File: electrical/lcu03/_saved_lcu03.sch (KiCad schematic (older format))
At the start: 94 parts, among them P1 screw, P10 swd, P11 stepper_conn, P12 stepper_conn, P13 stepper_conn, P16 screw, P17 screw, P2 screw, P3 screw, P4 screw, P5 ext-1, P6 ~rst~, P7 mode, P8 ext-2, P9 USB_B, Q1 bc857, Q2 bc847, Q3 bc857, Q4 ntd18n06l, U1 crystal-4pin, U2 CP2102, U3 m24c02, U4 NCP3063, U6 ts881, U7 lb1930mc

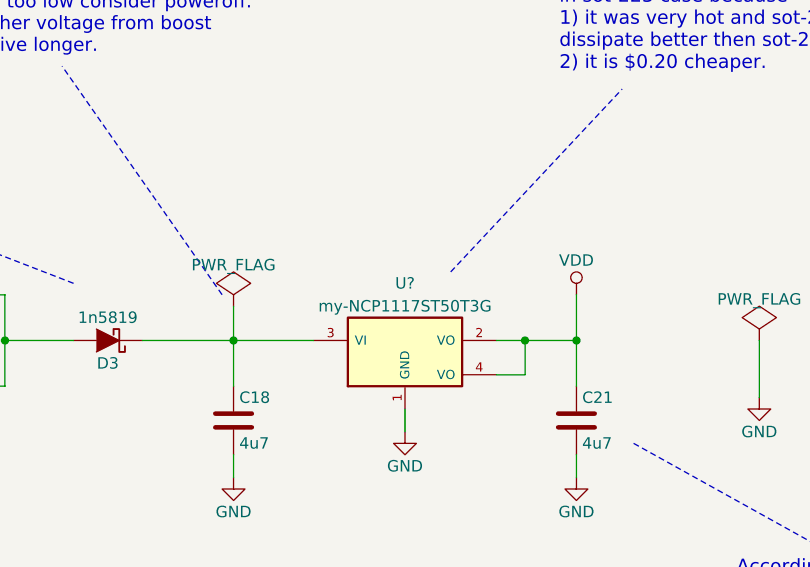
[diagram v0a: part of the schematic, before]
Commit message: Replaced linear regulator, changed socket footprints and implemented all improvements from "zzz.txt" file.
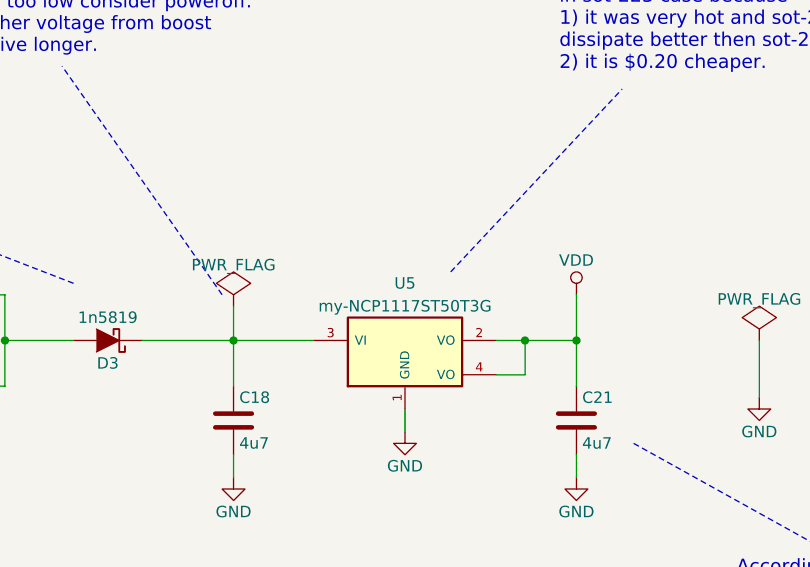
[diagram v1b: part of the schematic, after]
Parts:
- U5: renamed from U?; footprint (none) -> TO_SOT_Packages_SMD:SOT-223
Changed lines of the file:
@@
 According to datasheet \nthis one is mandatory \nfor stability.
 $Comp
-L my-NCP1117ST50T3G U?
+L my-NCP1117ST50T3G U5
 U 1 1 56BBB7F9
 P 15300 17250
-F 0 "U?" H 15300 17550 50  0000 C CNN
+F 0 "U5" H 15300 17550 50  0000 C CNN
 F 1 "my-NCP1117ST50T3G" H 15300 17450 50  0000 C CNN
-F 2 "" H 15300 17250 50  0000 C CNN
+F 2 "TO_SOT_Packages_SMD:SOT-223" H 15300 17250 50  0001 C CNN
 F 3 "" H 15300 17250 50  0000 C CNN
 	1    15300 17250

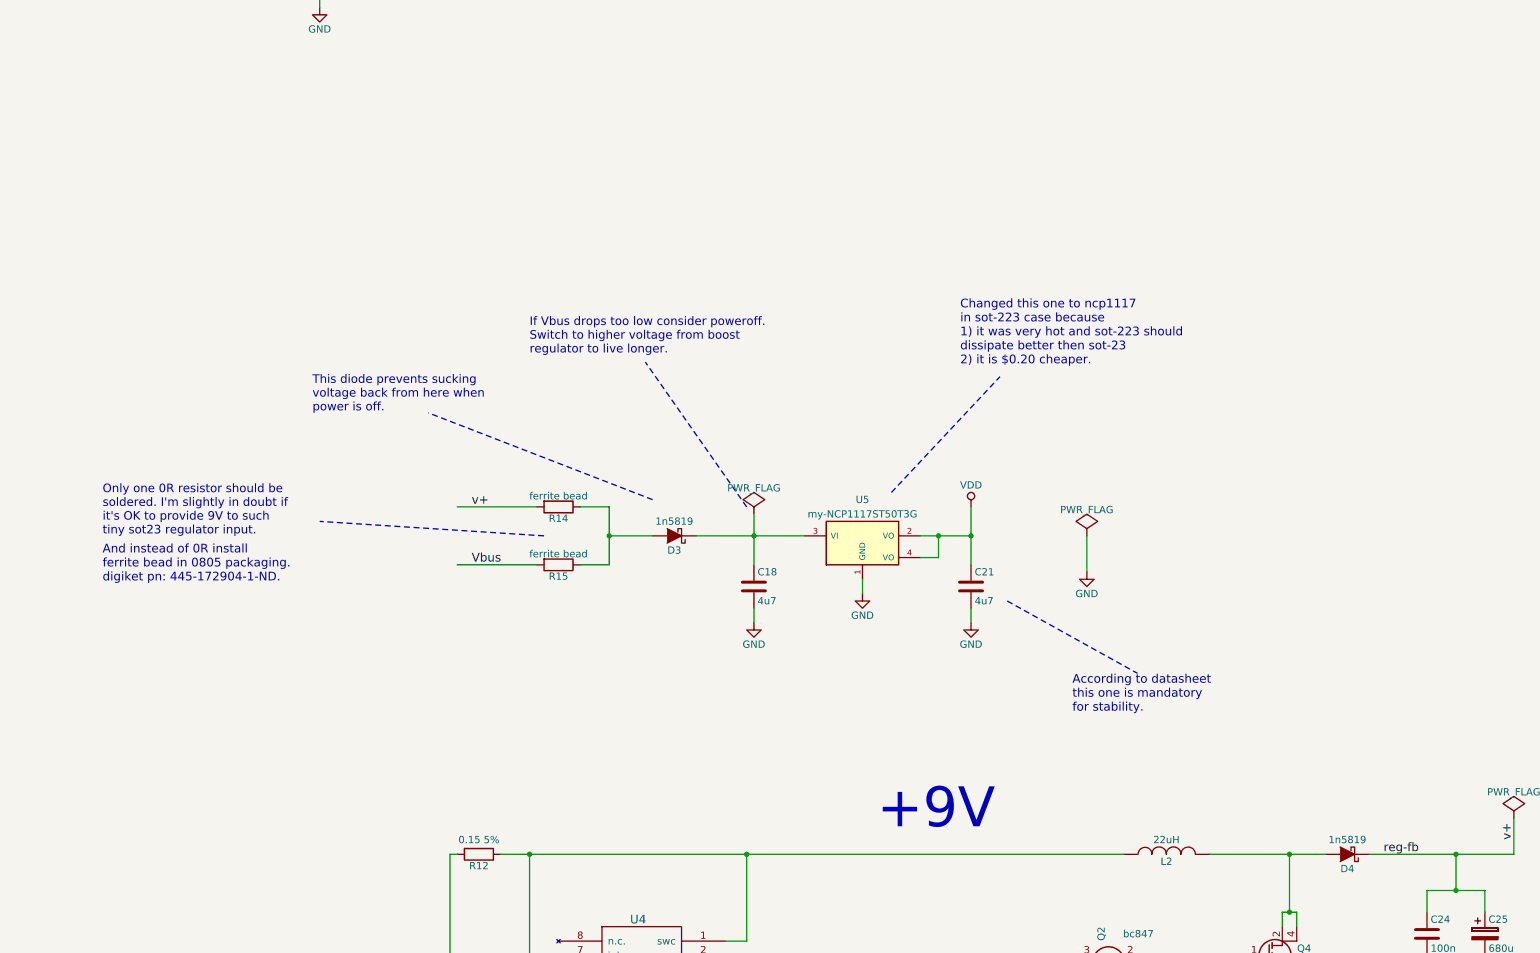
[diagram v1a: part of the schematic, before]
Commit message: Finished routing. Going to apply a few beautifications.
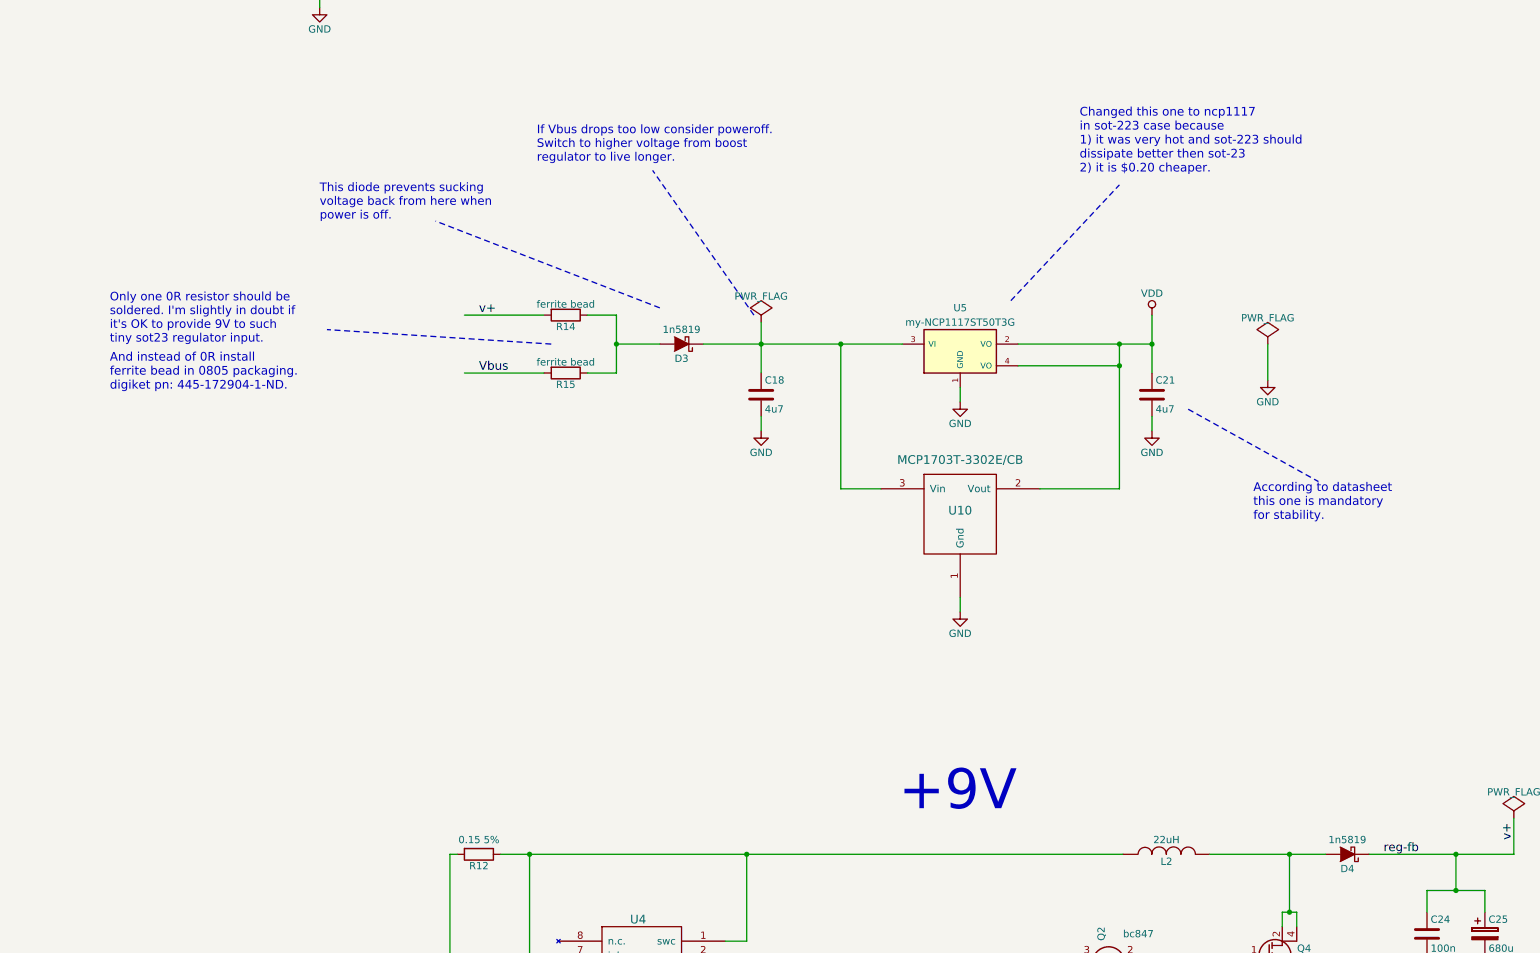
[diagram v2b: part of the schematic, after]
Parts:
- added U10: MCP1703T-3302E/CB, TO_SOT_Packages_SMD:SOT-23, symbol MCP1703T-3302E/CB
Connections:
- wire segments 368 -> 372
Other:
- moved on the sheet: C18, C21, D3, R14, R15, U5
